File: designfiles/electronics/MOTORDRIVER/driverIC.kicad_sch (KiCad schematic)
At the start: 59 parts, among them U4 TMC4671-LA

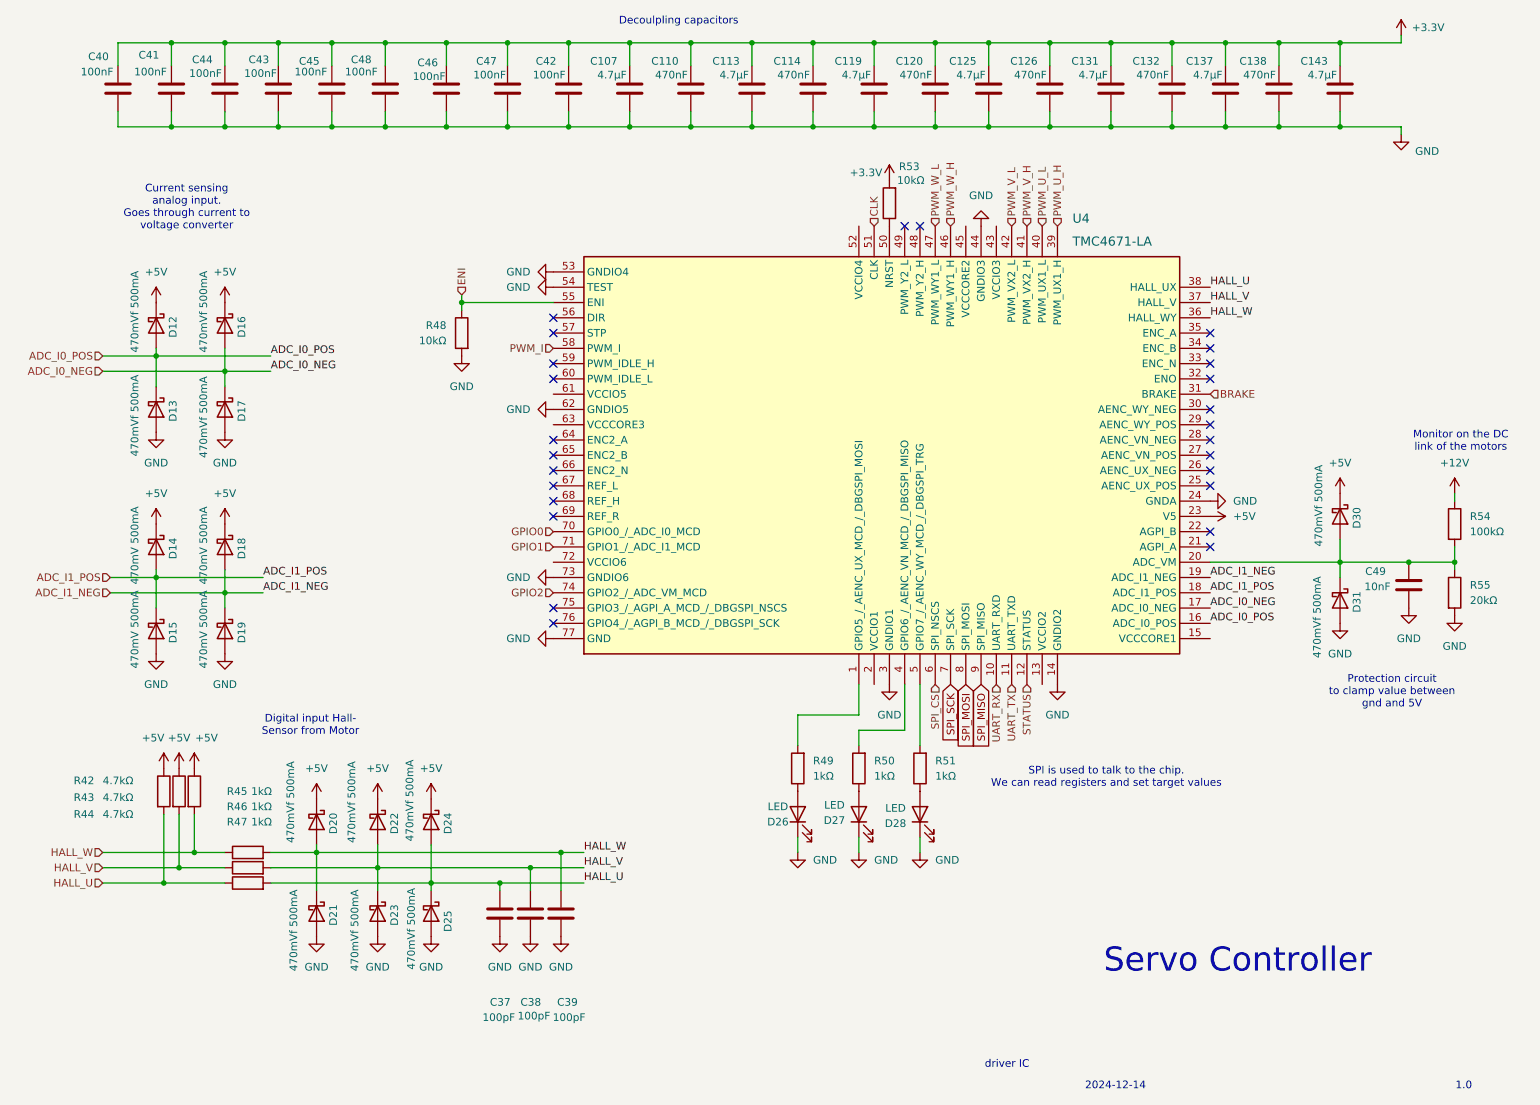
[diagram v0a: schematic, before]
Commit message: made clearer foldernames and cleaned up
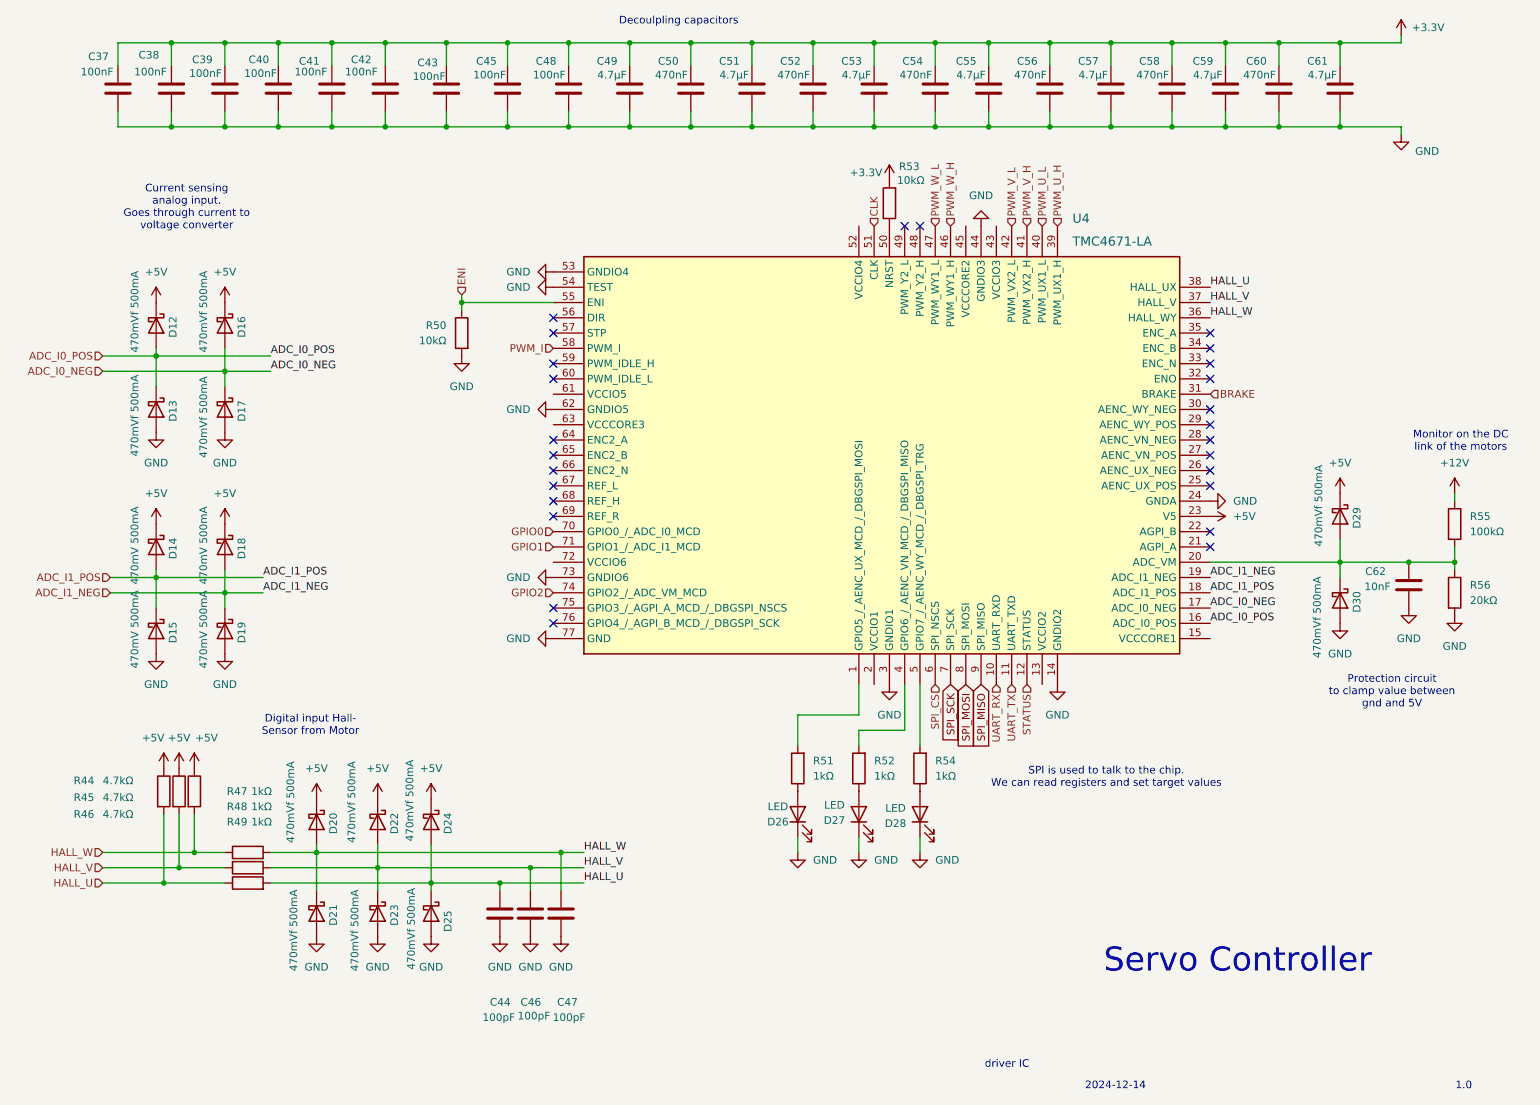
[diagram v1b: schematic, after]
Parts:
- renumbered C40 to C37, C41 to C38, C44 to C39, C43 to C40, C45 to C41, C48 to C42, C46 to C43, C37 to C44, C47 to C45, C38 to C46, C39 to C47, C42 to C48, C107 to C49, C110 to C50, C113 to C51, C114 to C52, C119 to C53, C120 to C54, C125 to C55, C126 to C56, C131 to C57, C132 to C58, C137 to C59, C138 to C60, C143 to C61, C49 to C62, D30 to D29, D31 to D30, R42 to R44, R43 to R45, R44 to R46, R45 to R47, R46 to R48, R47 to R49, R48 to R50, R49 to R51, R50 to R52, R51 to R54, R54 to R55, R55 to R56

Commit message: removed backup files and found components for special resistors and diodes
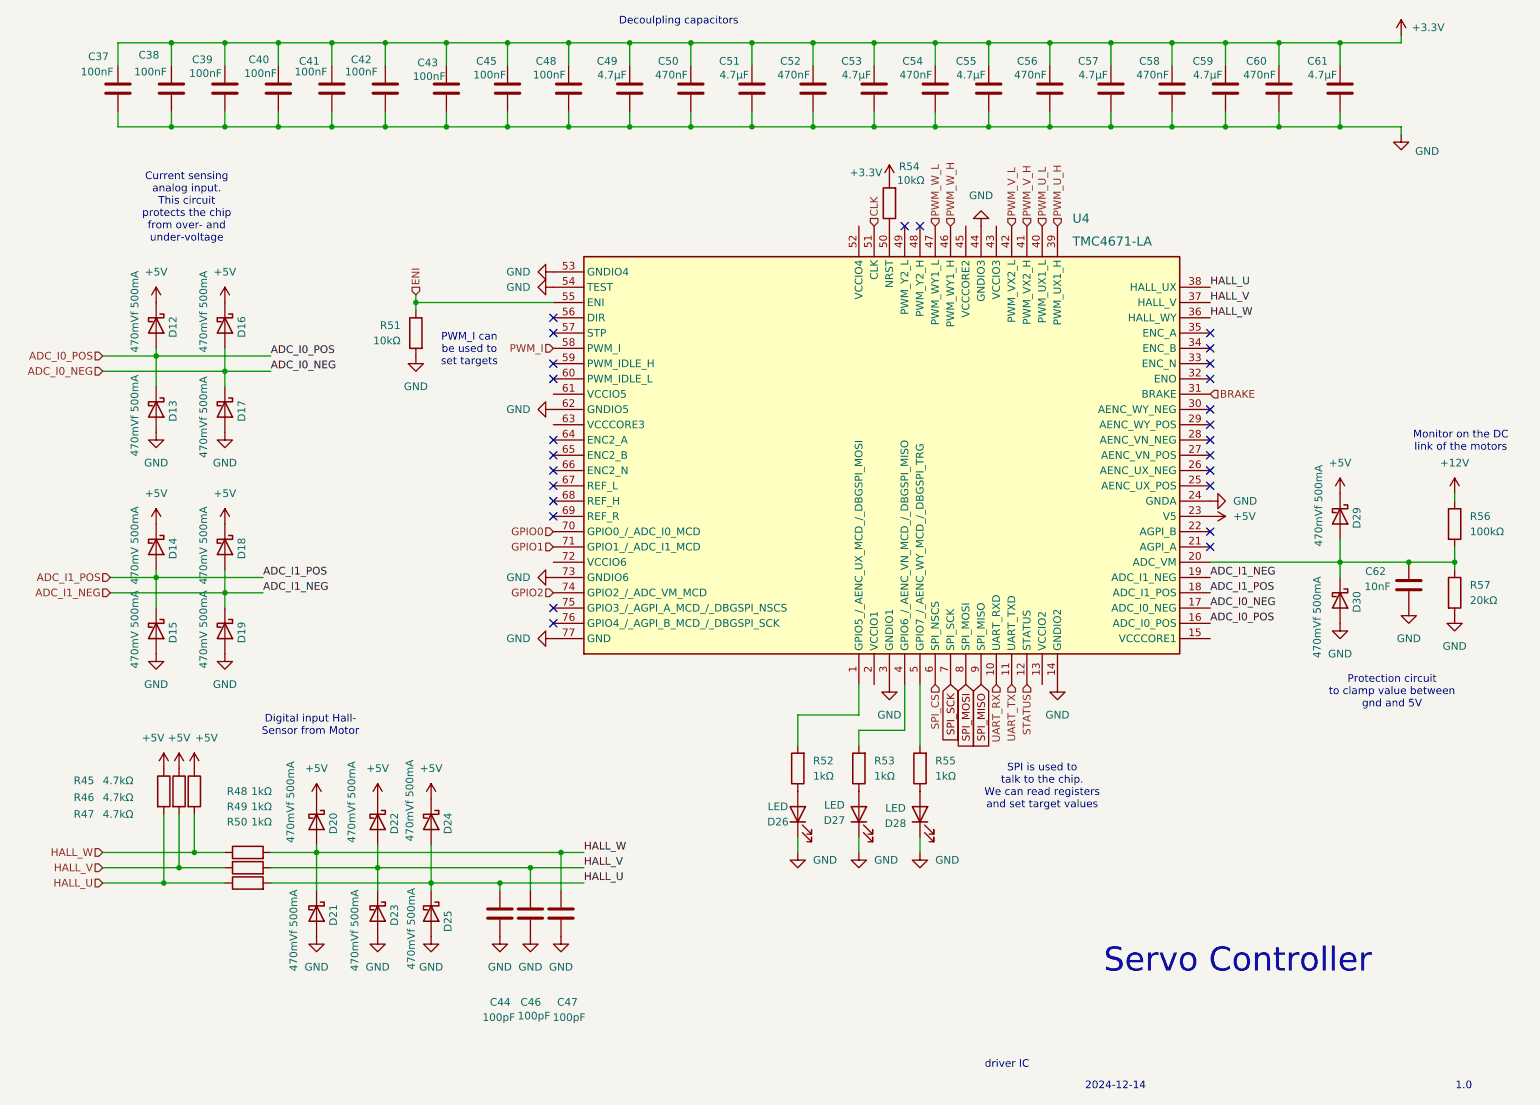
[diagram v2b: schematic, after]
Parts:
- renumbered R44 to R45, R45 to R46, R46 to R47, R47 to R48, R48 to R49, R49 to R50, R50 to R51, R51 to R52, R52 to R53, R53 to R54, R54 to R55, R55 to R56, R56 to R57
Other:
- note added: "Current sensing analog input. This circuit protects the chip from over- and under-voltage"
- note added: "PWM_I can be used to set targets"
- note removed: "Current sensing analog input. Goes through current to voltage converter"
- moved on the sheet: R51

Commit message: added diodes
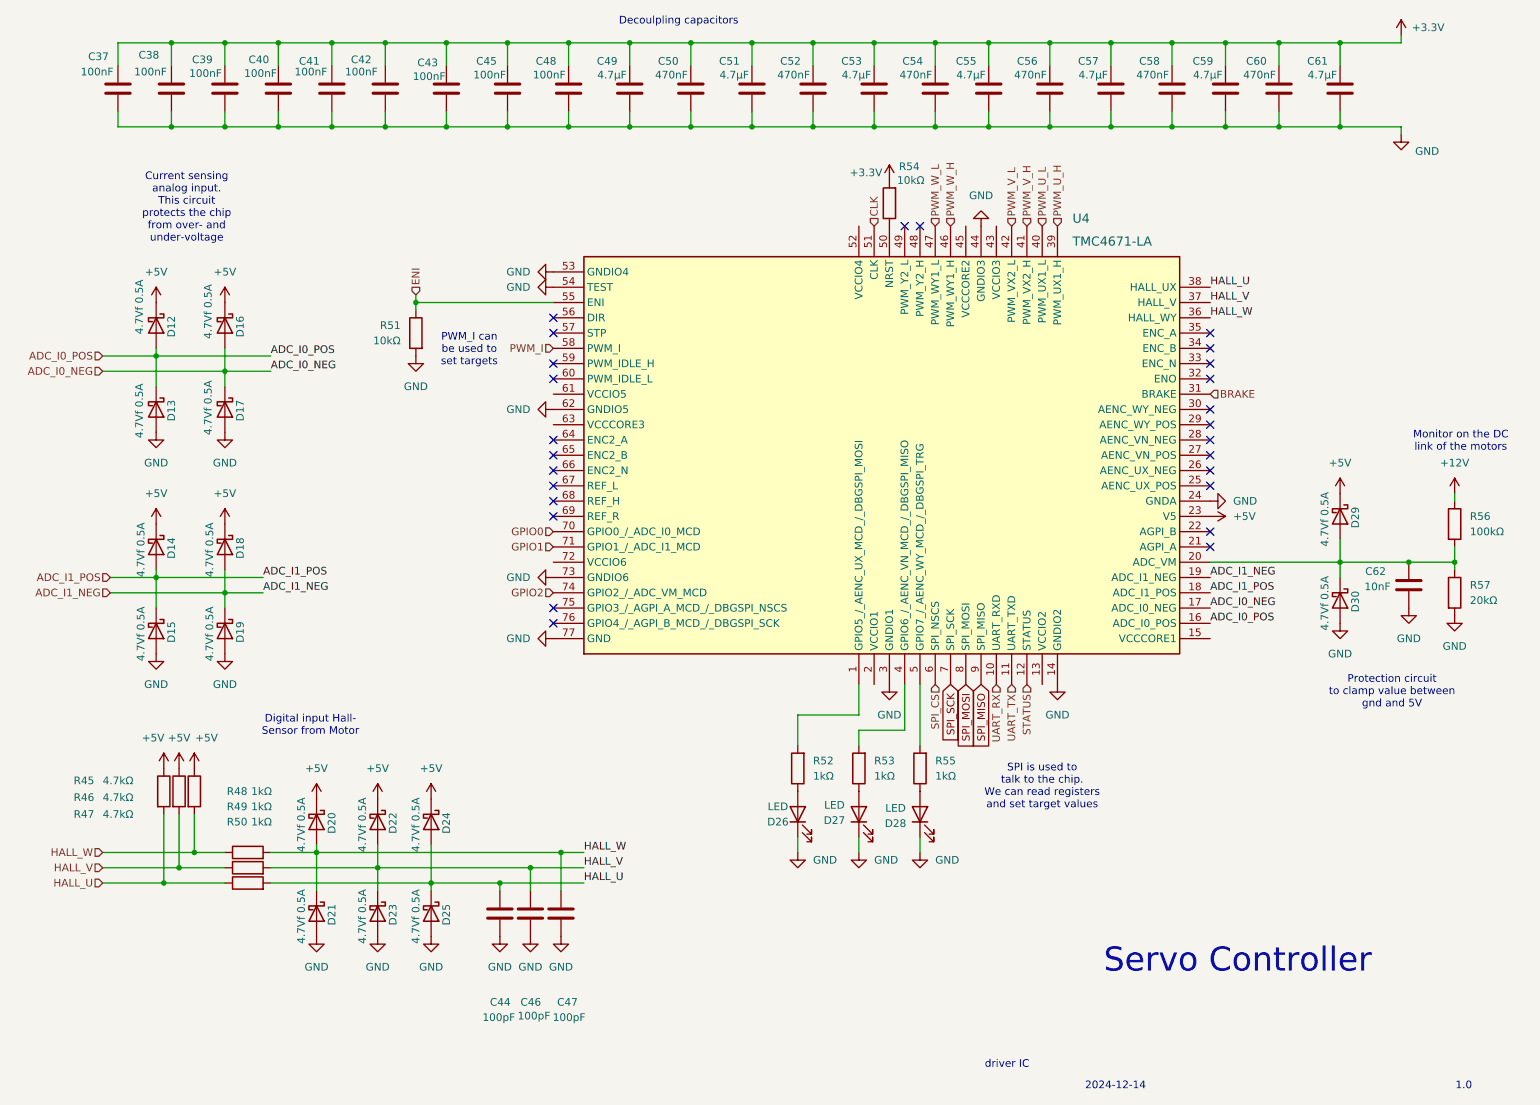
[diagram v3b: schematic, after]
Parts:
- D12, D13, D16, D17, D20, D21, D22, D23, D24, D25, D29, D30: value 470mVf 500mA -> 4.7Vf 0.5A; footprint Diode_SMD:D_0603_1608Metric -> kuben-footprints:DIOC1709X85N; Height (none) -> 0.85; Manufacturer_Name (none) -> Comchip Technology; Manufacturer_Part_Number (none) -> CDBU0520; Mouser Part Number (none) -> 750-CDBU0520; Mouser Price/Stock (none) -> https://www.mouser.co.uk/ProductDetail/Comchip-Technology/C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
- D14, D15, D18, D19: value 470mV 500mA -> 4.7Vf 0.5A; footprint Diode_SMD:D_0603_1608Metric -> kuben-footprints:DIOC1709X85N; Height (none) -> 0.85; Manufacturer_Name (none) -> Comchip Technology; Manufacturer_Part_Number (none) -> CDBU0520; Mouser Part Number (none) -> 750-CDBU0520; Mouser Price/Stock (none) -> https://www.mouser.co.uk/ProductDetail/Comchip-Technology/C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

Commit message: fixed root folder schematics
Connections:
- net CLK renamed SERVO_CLK
- net ENI renamed SERVO_ENI
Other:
- note added: "Decoupling capacitors"
- note removed: "Decoulpling capacitors"
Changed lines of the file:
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@@
 		)
 	)
-	(text "Decoulpling capacitors\n"
+	(text "Decoupling capacitors\n"
 		(exclude_from_sim no)
 		(at 140.208 16.764 0)
@@
 		)
 	)
+	(global_label "SERVO_CLK"
+		(shape input)
+		(at 172.72 50.8 90)
+		(fields_autoplaced yes)
+		(effects
+			(font
+				(size 1.27 1.27)
+			)
+			(justify left)
+		)
+		(property "Intersheetrefs" "${INTERSHEET_REFS}"
+			(at 172.72 38.4338 90)
+			(effects
+				(font
+					(size 1.27 1.27)
+				)
+				(justify left)
+				(hide yes)
+			)
+		)
+	)
 	(global_label "SPI_MISO"
 		(shape input)
@@
 		)
 	)
+	(global_label "SERVO_ENI"
+		(shape input)
+		(at 96.52 62.23 90)
+		(fields_autoplaced yes)
+		(effects
+			(font
+				(size 1.27 1.27)
+			)
+			(justify left)
+		)
+		(property "Intersheetrefs" "${INTERSHEET_REFS}"
+			(at 96.52 49.8638 90)
+			(effects
+				(font
+					(size 1.27 1.27)
+				)
+				(justify left)
+				(hide yes)
+			)
+		)
+	)
 	(hierarchical_label "ADC_I0_POS"
 		(shape input)
@@
 		)
 	)
-	(hierarchical_label "ENI"
-		(shape input)
-		(at 96.52 62.23 90)
-		(fields_autoplaced yes)
-		(effects
-			(font
-				(size 1.27 1.27)
-			)
-			(justify left)
-		)
-	)
 	(hierarchical_label "PWM_I"
 		(shape input)
@@
 		)
 	)
-	(hierarchical_label "CLK"
-		(shape input)
-		(at 172.72 50.8 90)
-		(fields_autoplaced yes)
-		(effects
-			(font
-				(size 1.27 1.27)
-			)
-			(justify left)
-		)
-	)
 	(hierarchical_label "PWM_U_H"
 		(shape input)
@@
 		)
 		(property "Value" "+3.3V"
-			(at 168.656 41.91 0)
+			(at 172.466 37.846 0)
 			(effects
 				(font
